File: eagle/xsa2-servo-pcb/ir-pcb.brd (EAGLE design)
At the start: 160 x 100 mm, 7 parts, among them IC1 ATMEGA328P-AU, IC2 PL-IRM0101, IC3 PL-IRM0101, IC4 PL-IRM0101, IC5 PL-IRM0101, IC6 PL-IRM0101, IC7 PL-IRM0101

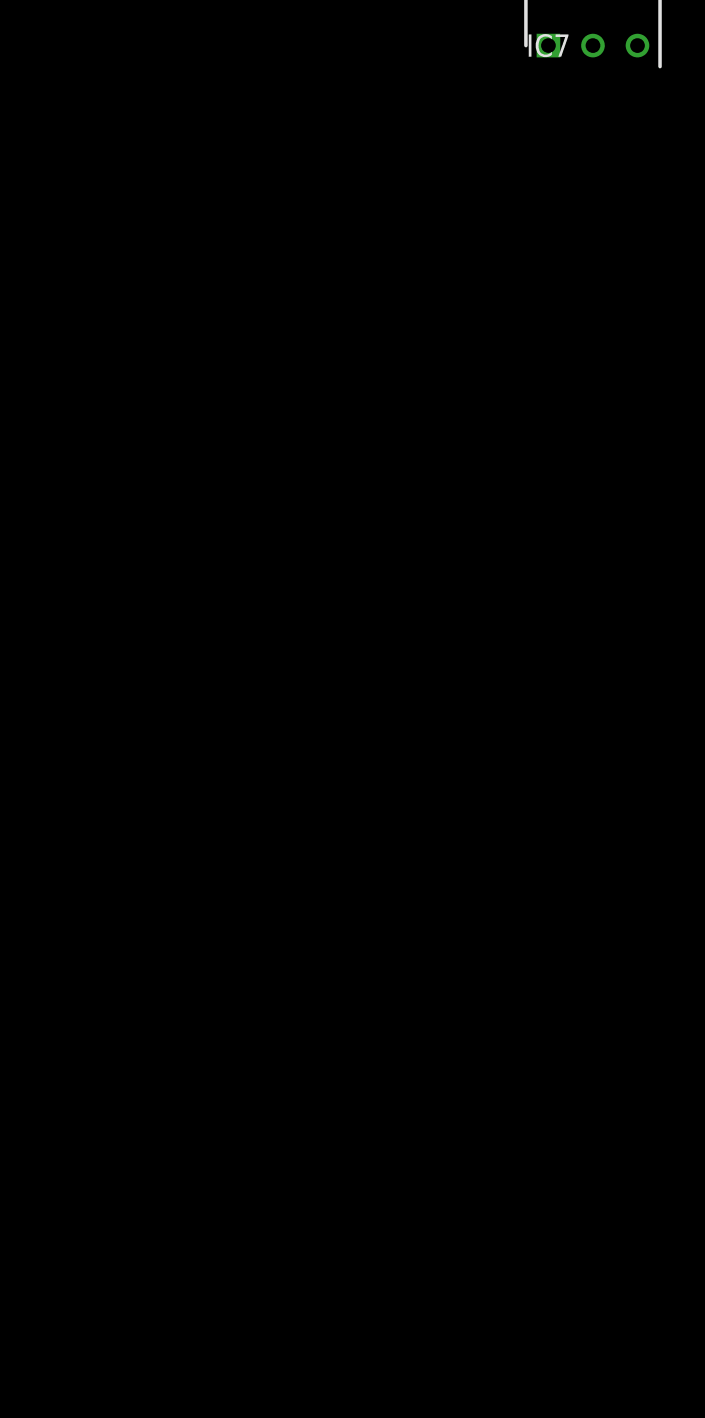
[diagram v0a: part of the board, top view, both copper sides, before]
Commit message: [eagle] 部品追加
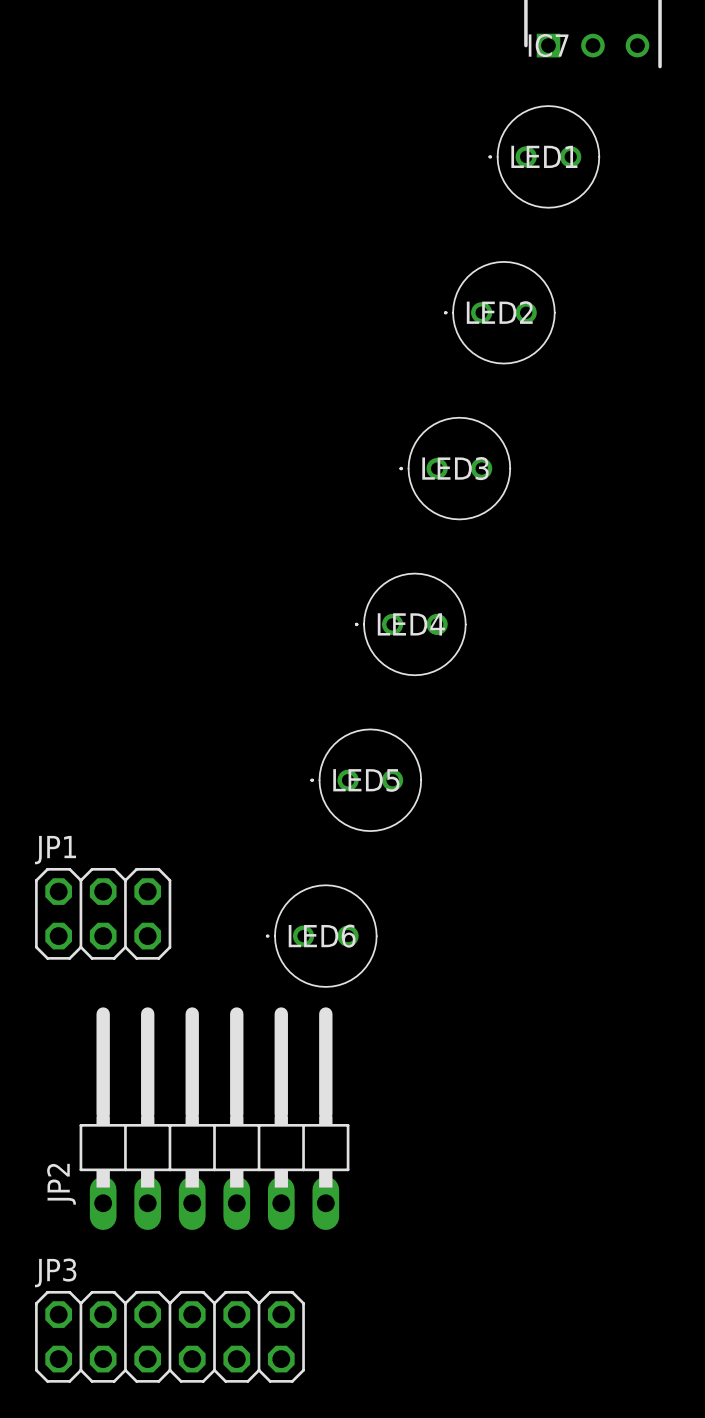
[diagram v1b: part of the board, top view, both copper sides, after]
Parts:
- added JP1: (no value), pinhead:2X03
- added JP2: (no value), pinhead:1X06/90
- added JP3: (no value), pinhead:2X06
- added LED1, LED2, LED3, LED4, LED5, LED6: OSI5FU5111C-40, SamacSys_Parts:OSI5FU5111C40
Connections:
- new net +3V3: IC2.3, IC3.3, IC4.3, IC5.3, IC6.3, IC7.3, JP1.2, JP2.3
- new net GND: IC2.2, IC3.2, IC4.2, IC5.2, IC6.2, IC7.2, JP1.6, JP2.1, JP2.2
- new net N$1: IC1.16, JP1.1
- new net N$2: IC1.15, JP1.4
- new net N$3: IC1.29, JP1.5
- new net N$4: IC1.2, IC2.1, IC3.1, IC4.1, IC5.1, IC6.1, IC7.1
- new net N$5: IC1.17, JP1.3

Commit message: [eagle] 基板設計追加
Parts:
- added C1, C2: 0.1u, rcl:C0603
- added Q1: IRLML6402, SamacSys_Parts:SOT95P237X112-3N
- added Q2, Q3, Q4: IRFML8244, SamacSys_Parts:SOT95P237X112-3N
- added Q5, Q6, Q7: 2SC2712-GR_F_, SamacSys_Parts:SSM3K7002CFULF
- added R1, R6: 1k, rcl:R0603
- added R2, R3: 1, rcl:R0603
- added R4: 2, rcl:R0603
- added R5: 10, rcl:R0603
- added Y1: MA-506_8.0000M-D3__ROHS, SamacSys_Parts:MA50680000MD3ROHS
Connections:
- removed net AVCC: IC1.18
- removed net GND_1: IC1.3
- removed net GND_2: IC1.5
- removed net GND_3: IC1.21
- removed net VCC_1: IC1.4
- removed net VCC_2: IC1.6
- new net N$10: IC1.1, Q1.1, R1.2
- new net N$12: LED3.2, LED6.2, R2.2, R3.2, R4.2, R5.2
- new net N$13: C2.2, IC1.20
- new net N$14: IC1.27, JP3.2
- new net N$15: Q2.3, R2.1, R3.1
- new net N$16: Q3.3, R4.1
- new net N$17: Q4.3, R5.1
- new net N$18: IC1.9, Q2.1
- new net N$19: IC1.10, Q3.1
- new net N$20: IC1.11, Q4.1
- new net N$21: IC1.28, JP3.3
- new net N$22: IC1.7, Y1.2, Y1.3
- new net N$23: IC1.30, JP2.4, JP3.4
- new net N$24: IC1.31, JP2.5, JP3.5
- new net N$25: C1.2, JP2.6
- new net N$26: IC1.8, Y1.1, Y1.4
- new net N$4: LED1.1, LED4.1, Q1.3, R6.2
- new net N$6: LED1.2, LED2.1
- new net N$7: LED2.2, LED3.1
- new net N$8: LED4.2, LED5.1
- new net N$9: LED5.2, LED6.1
- new net VDD: JP3.12, Q1.2, R1.1
- net +3V3: now also IC1.18, IC1.4, IC1.6, JP3.7
- net GND: now also C2.1, IC1.21, IC1.3, IC1.5, JP3.1, Q2.2, Q3.2, Q4.2, R6.1
- net N$3: now also C1.1, JP3.6

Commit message: [eagle] 回路追加
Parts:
- removed Q6, Q7: 2SC2712-GR_F_, SamacSys_Parts:SSM3K7002CFULF
- removed Y1: MA-506_8.0000M-D3__ROHS, SamacSys_Parts:MA50680000MD3ROHS
- added C3, C4: 22p, rcl:C0603
- added C5: 0.1u, rcl:C0603
- added C7: 16S-VP82M, SamacSys_Parts:16SVF270M
- added R7: 10k, rcl:R0603
- added R8: 1, rcl:R0603
- added S1: IS-2235, SamacSys_Parts:IS2235
- JP1: value (none) -> AVR ISP
- JP2: value (none) -> FTDI Basic
- JP3: value (none) -> Stacking Connector
- Q5: value 2SC2712-GR_F_ -> 8MHz; device SamacSys_Parts:SSM3K7002CFULF -> special:QS
- moved Q5 25.9 mm to (-55.9, -233.7)
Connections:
- new net N$27: C7.1, Q1.2, R1.1, R8.1
- new net N$28: C1.1, JP2.6, S1.6
- new net N$29: JP3.5, S1.2
- net +3V3: now also C5.2, R7.1
- net GND: now also C3.1, C4.1, C5.1, C7.2
- net N$22: now also C3.2, Q5.1; no longer Y1.2, Y1.3
- net N$24: now also S1.3; no longer JP3.5
- net N$25: now also IC1.29, JP1.5, R7.2; no longer JP2.6
- net N$26: now also C4.2, Q5.2; no longer Y1.1, Y1.4
- net N$3: now also S1.5; no longer C1.1, IC1.29, JP1.5
- net VDD: now also R8.2; no longer Q1.2, R1.1

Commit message: [eagle] AVRの赤外受光ピンを変更
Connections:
- removed net N$2: IC1.15, JP1.4
- net N$11: now also IC1.15, JP1.4; no longer IC1.2
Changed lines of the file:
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@@
 <wire x1="9.15" y1="-10.6" x2="-31.75" y2="-99.06" width="0" layer="19" extent="1-1"/>
-</signal>
-<signal name="N$2">
-<contactref element="IC1" pad="15"/>
-<contactref element="JP1" pad="4"/>
-<wire x1="8.35" y1="-10.6" x2="-29.21" y2="-96.52" width="0" layer="19" extent="1-1"/>
 </signal>
 <signal name="+3V3">
@@
 <contactref element="IC5" pad="1"/>
 <contactref element="IC6" pad="1"/>
-<contactref element="IC1" pad="2"/>
+<contactref element="IC1" pad="15"/>
+<contactref element="JP1" pad="4"/>
+<wire x1="-3.81" y1="-48.26" x2="-29.21" y2="-96.52" width="0" layer="19" extent="1-1"/>
 <wire x1="-2.54" y1="-41.91" x2="-3.81" y2="-48.26" width="0" layer="19" extent="1-1"/>
 <wire x1="-1.27" y1="-35.56" x2="-2.54" y2="-41.91" width="0" layer="19" extent="1-1"/>
@@
 <wire x1="1.27" y1="-22.86" x2="0" y2="-29.21" width="0" layer="19" extent="1-1"/>
 <wire x1="2.54" y1="-16.51" x2="1.27" y2="-22.86" width="0" layer="19" extent="1-1"/>
-<wire x1="2.1" y1="-4.35" x2="2.54" y2="-16.51" width="0" layer="19" extent="1-1"/>
+<wire x1="8.35" y1="-10.6" x2="2.54" y2="-16.51" width="0" layer="19" extent="1-1"/>
 </signal>
 <signal name="N$4">

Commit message: [eagle] 赤外発光部のPMOSにNMOSを追加
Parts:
- added C6: 16S-VP82M, SamacSys_Parts:16SVF270M
- added Q6: IRFML8244, SamacSys_Parts:SOT95P237X112-3N
- added R9: 1k, rcl:R0603
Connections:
- new net N$2: Q1.1, Q6.3, R1.2
- net GND: now also C6.2, Q6.2, R9.1
- net N$10: now also Q6.1, R9.2; no longer Q1.1, R1.2
- net N$27: now also C6.1
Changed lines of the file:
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@@
 <attribute name="VALUE" x="-55.88" y="-271.78" size="1.27" layer="27" align="center"/>
+</element>
+<element name="Q6" library="SamacSys_Parts" package="SOT95P237X112-3N" value="IRFML8244" x="-58.42" y="-279.4" smashed="yes">
+<attribute name="ARROW_PART_NUMBER" value="" x="-58.42" y="-279.4" size="1.778" layer="27" display="off"/>
+<attribute name="ARROW_PRICE-STOCK" value="" x="-58.42" y="-279.4" size="1.778" layer="27" display="off"/>
+<attribute name="DESCRIPTION" value="HEXFET Power MOSFET  25V" x="-58.42" y="-279.4" size="1.778" layer="27" display="off"/>
+<attribute name="HEIGHT" value="1.12mm" x="-58.42" y="-279.4" size="1.778" layer="27" display="off"/>
+<attribute name="MANUFACTURER_NAME" value="Infineon" x="-58.42" y="-279.4" size="1.778" layer="27" display="off"/>
+<attribute name="MANUFACTURER_PART_NUMBER" value="IRFML8244" x="-58.42" y="-279.4" size="1.778" layer="27" display="off"/>
+<attribute name="MOUSER_PART_NUMBER" value="N/A" x="-58.42" y="-279.4" size="1.778" layer="27" display="off"/>
+<attribute name="MOUSER_PRICE-STOCK" value="https://www.mouser.co.uk/ProductDetail/Infineon-Technologies/IRFML8244?qs=bAKSY%2FctAC4ez%2FysLA2f0A%3D%3D" x="-58.42" y="-279.4" size="1.778" layer="27" display="off"/>
+<attribute name="NAME" x="-58.42" y="-279.4" size="1.27" layer="25" align="center"/>
+<attribute name="VALUE" x="-58.42" y="-279.4" size="1.27" layer="27" align="center"/>
+</element>
+<element name="R9" library="rcl" library_urn="urn:adsk.eagle:library:334" package="R0603" package3d_urn="urn:adsk.eagle:package:23555/3" value="1k" x="-60.96" y="-284.48" smashed="yes">
+<attribute name="NAME" x="-61.595" y="-283.845" size="1.27" layer="25"/>
+<attribute name="POPULARITY" value="77" x="-60.96" y="-284.48" size="1.778" layer="27" display="off"/>
+<attribute name="SPICEPREFIX" value="R" x="-60.96" y="-284.48" size="1.778" layer="27" display="off"/>
+<attribute name="VALUE" x="-61.595" y="-286.385" size="1.27" layer="27"/>
+</element>
+<element name="C6" library="SamacSys_Parts" package="16SVF270M" value="16S-VP82M" x="-55.88" y="-292.1" smashed="yes">
+<attribute name="ARROW_PART_NUMBER" value="" x="-55.88" y="-292.1" size="1.778" layer="27" display="off"/>
+<attribute name="ARROW_PRICE-STOCK" value="" x="-55.88" y="-292.1" size="1.778" layer="27" display="off"/>
+<attribute name="DESCRIPTION" value="Panasonic 82uF 16 V Polymer Aluminium Electrolytic Capacitor E7, OS-CON Series 2000h 8 x 6.9mm" x="-55.88" y="-292.1" size="1.778" layer="27" display="off"/>
+<attribute name="HEIGHT" value="7mm" x="-55.88" y="-292.1" size="1.778" layer="27" display="off"/>
+<attribute name="MANUFACTURER_NAME" value="Panasonic" x="-55.88" y="-292.1" size="1.778" layer="27" display="off"/>
+<attribute name="MANUFACTURER_PART_NUMBER" value="16S-VP82M" x="-55.88" y="-292.1" size="1.778" layer="27" display="off"/>
+<attribute name="MOUSER_PART_NUMBER" value="" x="-55.88" y="-292.1" size="1.778" layer="27" display="off"/>
+<attribute name="MOUSER_PRICE-STOCK" value="" x="-55.88" y="-292.1" size="1.778" layer="27" display="off"/>
+<attribute name="NAME" x="-55.88" y="-292.1" size="1.27" layer="25" align="center"/>
+<attribute name="VALUE" x="-55.88" y="-292.1" size="1.27" layer="27" align="center"/>
 </element>
 </elements>
@@
 <contactref element="C5" pad="1"/>
 <contactref element="C7" pad="2"/>
+<contactref element="Q6" pad="2"/>
+<contactref element="R9" pad="1"/>
+<contactref element="C6" pad="2"/>
 <wire x1="-50.38" y1="-184.15" x2="-50.38" y2="-194.31" width="0" layer="19" extent="1-1"/>
 <wire x1="-48.04" y1="-174.94" x2="-50.38" y2="-184.15" width="0" layer="19" extent="1-1"/>
@@
 <wire x1="-61.81" y1="-254" x2="-61.81" y2="-243.84" width="0" layer="19" extent="1-1"/>
 <wire x1="-52.405" y1="-271.78" x2="-61.81" y2="-254" width="0" layer="19" extent="1-1"/>
+<wire x1="-59.47" y1="-280.35" x2="-52.405" y2="-271.78" width="0" layer="19" extent="1-1"/>
+<wire x1="-61.81" y1="-284.48" x2="-59.47" y2="-280.35" width="0" layer="19" extent="1-1"/>
+<wire x1="-52.405" y1="-292.1" x2="-61.81" y2="-284.48" width="0" layer="19" extent="1-1"/>
 <wire x1="-31.75" y1="-123.19" x2="-45.5" y2="-167.32" width="0" layer="19" extent="1-1"/>
 <wire x1="-29.21" y1="-114.3" x2="-31.75" y2="-123.19" width="0" layer="19" extent="1-1"/>
@@
 <signal name="N$10">
 <contactref element="IC1" pad="1"/>
-<contactref element="R1" pad="2"/>
-<contactref element="Q1" pad="1"/>
-<wire x1="-30.9" y1="-127" x2="-45.5" y2="-161.61" width="0" layer="19" extent="1-1"/>
-<wire x1="2.1" y1="-3.55" x2="-30.9" y2="-127" width="0" layer="19" extent="1-1"/>
+<contactref element="Q6" pad="1"/>
+<contactref element="R9" pad="2"/>
+<wire x1="-59.47" y1="-278.45" x2="-60.11" y2="-284.48" width="0" layer="19" extent="1-1"/>
+<wire x1="2.1" y1="-3.55" x2="-59.47" y2="-278.45" width="0" layer="19" extent="1-1"/>
 </signal>
 <signal name="N$11">
@@
 <contactref element="R8" pad="1"/>
 <contactref element="C7" pad="1"/>
+<contactref element="C6" pad="1"/>
 <wire x1="-32.6" y1="-127" x2="-45.5" y2="-163.51" width="0" layer="19" extent="1-1"/>
 <wire x1="-61.81" y1="-259.08" x2="-45.5" y2="-163.51" width="0" layer="19" extent="1-1"/>
 <wire x1="-59.355" y1="-271.78" x2="-61.81" y2="-259.08" width="0" layer="19" extent="1-1"/>
+<wire x1="-59.355" y1="-292.1" x2="-59.355" y2="-271.78" width="0" layer="19" extent="1-1"/>
+</signal>
+<signal name="N$2">
+<contactref element="R1" pad="2"/>
+<contactref element="Q1" pad="1"/>
+<contactref element="Q6" pad="3"/>
+<wire x1="-30.9" y1="-127" x2="-45.5" y2="-161.61" width="0" layer="19" extent="1-1"/>
+<wire x1="-57.37" y1="-279.4" x2="-45.5" y2="-161.61" width="0" layer="19" extent="1-1"/>
 </signal>
 </signals>

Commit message: [eagle] 連結コネクタのピン数を増加
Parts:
- added C10, C11, C12, C13, C14, C15, C16, C17, C18, C19, C8, C9: 0.1u, rcl:C0603
- added IC10, IC11, IC12, IC13, IC14, IC15, IC16, IC17, IC18, IC19, IC8, IC9: SK6812_SIDE, SamacSys_Parts:SK6812SIDE
- added R10, R11: 0, rcl:R0603
- JP2: device pinhead:1X06/90 -> pinhead:1X06
- JP3: device pinhead:2X06 -> pinhead:2X07
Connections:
- new net N$30: IC1.27, JP3.3
- new net N$31: IC10.1, IC9.3
- new net N$32: IC10.3, IC11.1
- new net N$33: IC11.3, IC12.1
- new net N$34: IC12.3, IC13.1
- new net N$35: IC13.3, IC14.1
- new net N$36: IC14.3, IC15.1
- new net N$37: IC15.3, IC16.1
- new net N$38: IC16.3, IC17.1
- new net N$39: IC17.3, IC18.1
- new net N$40: IC18.3, IC19.1
- new net N$42: JP3.10, R10.2
- new net N$43: IC1.32, R11.2
- new net N$44: IC8.1, R10.1, R11.1
- net +3V3: now also JP3.8; no longer JP3.7
- net GND: now also C10.1, C11.1, C12.1, C13.1, C14.1, C15.1, C16.1, C17.1, C18.1, C19.1, C8.1, C9.1, IC10.4, IC11.4, IC12.4, IC13.4, IC14.4, IC15.4, IC16.4, IC17.4, IC18.4, IC19.4, IC8.4, IC9.4, JP3.2
- net N$14: now also JP3.7, S1.2; no longer IC1.27, JP3.2
- net N$21: now also JP3.4; no longer JP3.3
- net N$23: now also JP3.5; no longer JP3.4
- net N$24: now also IC8.3, IC9.1; no longer IC1.31, JP2.5, S1.3
- net N$28: now also S1.3; no longer S1.6
- net N$29: now also IC1.31, JP2.5, S1.6; no longer JP3.5, S1.2
- net VDD: now also C10.2, C11.2, C12.2, C13.2, C14.2, C15.2, C16.2, C17.2, C18.2, C19.2, C8.2, C9.2, IC10.2, IC11.2, IC12.2, IC13.2, IC14.2, IC15.2, IC16.2, IC17.2, IC18.2, IC19.2, IC8.2, IC9.2, JP3.11

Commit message: [eagle] IR基板のパターン設計
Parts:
- removed C6, C7: 16S-VP82M, SamacSys_Parts:16SVF270M
- removed JP2: FTDI Basic, pinhead:1X06
- removed R3, R8: 1, rcl:R0603
- removed R4: 2, rcl:R0603
- removed R5: 10, rcl:R0603
- added C20: 25PFV100M6.3X8, SamacSys_Parts:CAPAE660X800N
- added R12: 1, rcl:R2512W
- added R14: 2, rcl:R2512W
- added R15: 10, rcl:R2512W
- R2: value 1 -> 39; device rcl:R0603 -> rcl:R2512W
- moved C19 454.0 mm to (35.3, 38.0), flipped to the bottom, turned to 330 degrees
- moved R10 441.4 mm to (69.8, 10.2), flipped to the bottom
- moved R11 441.4 mm to (69.8, 5.08), flipped to the bottom
- moved C18 441.0 mm to (40.8, 28.5), flipped to the bottom, turned to 330 degrees
- moved C17 417.7 mm to (38.8, 9.98), flipped to the bottom, turned to 30 degrees
- moved C16 406.1 mm to (35.4, 3.94), flipped to the bottom, turned to 30 degrees
- moved C10 404.4 mm to (12.2, 38.1), flipped to the bottom, turned to 210 degrees
- moved C11 402.5 mm to (8.56, 31.8), flipped to the bottom, turned to 210 degrees
- moved IC19 402.1 mm to (38.1, 35.7), flipped to the bottom, turned to 240 degrees
- moved C15 399.1 mm to (32.7, 2.49), flipped to the bottom, turned to 90 degrees
- moved IC18 390.7 mm to (43.6, 26.1), flipped to the bottom, turned to 240 degrees
- moved C14 390.0 mm to (14.8, 2.49), flipped to the bottom, turned to 90 degrees
- moved C12 389.1 mm to (6.73, 13.5), flipped to the bottom, turned to 150 degrees
- moved C13 385.9 mm to (12.2, 3.96), flipped to the bottom, turned to 150 degrees
- moved IC17 377.2 mm to (43.6, 15.9), flipped to the bottom, turned to 300 degrees
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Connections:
- net +3V3: no longer JP2.3
- net GND: now also C20.2; no longer C6.2, C7.2, JP2.1, JP2.2
- net N$12: now also R14.2, R15.2; no longer R3.2, R4.2, R5.2
- net N$15: now also R14.1; no longer R2.1, R3.1
- net N$16: now also R15.1; no longer R4.1
- net N$17: now also R2.1; no longer R5.1
- net N$23: no longer JP2.4
- net N$27: now also C20.1, R12.1; no longer C6.1, C7.1, R8.1
- net N$28: no longer JP2.6
- net N$29: no longer JP2.5
- net VDD: now also R12.2; no longer R8.2
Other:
- board size 160 x 100 mm -> 96 x 85 mm

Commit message: [eagle] サーボ基板完成
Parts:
- removed JP1: AVR ISP, pinhead:2X03
- added J1: BM06B-SRSS-TBT_LF__SN_, SamacSys_Parts:BM06BSRSSTBTLFSN
- moved R12 36.5 mm to (28.5, 22.6), turned to 90 degrees
- moved Q1 28.3 mm to (57.4, 28.0), flipped to the top
- moved C20 8.51 mm to (21.6, 23.5), turned to 180 degrees
- moved Q4 3.81 mm to (18.2, 17.6)
- moved Q5 3.07 mm to (15.3, 14.0)
- moved C4 3.05 mm to (15.3, 14.9)
- moved C3 3.03 mm to (15.3, 13.1)
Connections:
- net +3V3: now also J1.2; no longer JP1.2
- net GND: now also J1.6; no longer JP1.6
- net N$1: now also J1.1; no longer JP1.1
- net N$25: now also J1.5; no longer JP1.5
- net N$41: now also J1.4; no longer JP1.4
- net N$5: now also J1.3; no longer JP1.3
